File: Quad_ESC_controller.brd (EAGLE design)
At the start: 25.8 x 34.2 mm, 27 parts, among them IC1 OP-AMP, Y1 ECS-80-S-4X

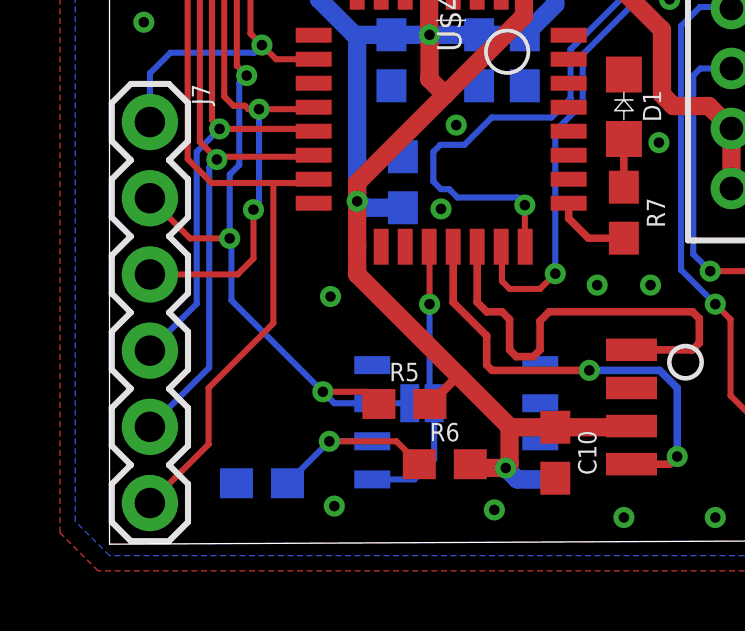
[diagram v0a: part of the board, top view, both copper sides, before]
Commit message: fixed stupid jumper under chip mistake
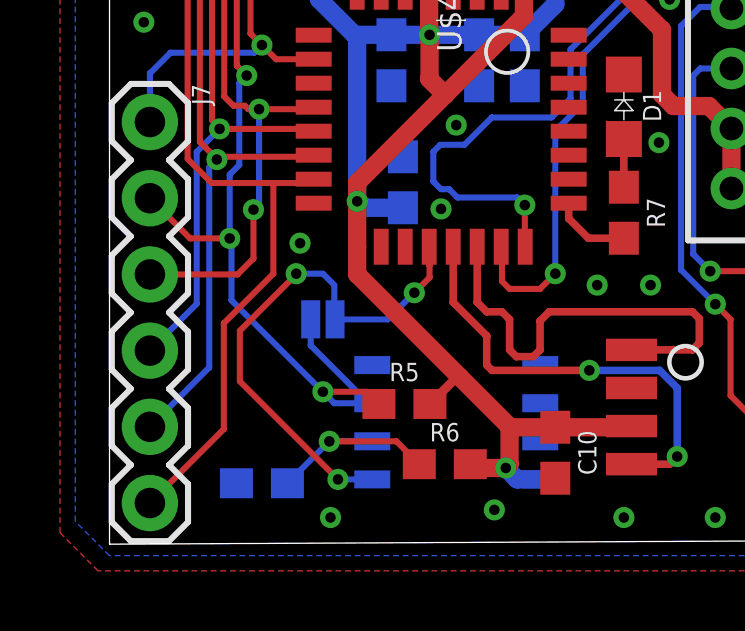
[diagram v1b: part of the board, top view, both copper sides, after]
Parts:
- moved JP1 4.33 mm to (7.11, 7.49)
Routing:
- net TLM: track 9.50 -> 17.5 mm, vias 1 -> 3
- net TLM_ESC: track 34.2 -> 36.7 mm
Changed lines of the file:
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@@
 <attribute name="VALUE" x="5.08" y="2.794" size="0.6096" layer="28" font="vector" ratio="20" rot="MR180" align="top-center"/>
 </element>
-<element name="JP1" library="SparkFun-Jumpers" library_urn="urn:adsk.eagle:library:528" package="SMT-JUMPER_2_NO_SILK" package3d_urn="urn:adsk.eagle:package:39279/1" value="JUMPER-SMT_2_NO_SILK" x="10.414" y="4.699" smashed="yes" rot="MR180">
-<attribute name="NAME" x="10.414" y="3.556" size="0.6096" layer="26" font="vector" ratio="20" rot="MR180" align="bottom-center"/>
+<element name="JP1" library="SparkFun-Jumpers" library_urn="urn:adsk.eagle:library:528" package="SMT-JUMPER_2_NO_SILK" package3d_urn="urn:adsk.eagle:package:39279/1" value="JUMPER-SMT_2_NO_SILK" x="7.112" y="7.493" smashed="yes" rot="MR180">
+<attribute name="NAME" x="7.112" y="6.35" size="0.6096" layer="26" font="vector" ratio="20" rot="MR180" align="bottom-center"/>
 </element>
 <element name="J7" library="SparkFun-Connectors" library_urn="urn:adsk.eagle:library:513" package="1X06" package3d_urn="urn:adsk.eagle:package:38009/1" value="" x="1.3462" y="14.0716" smashed="yes" rot="R270">
@@
 <via x="20.193" y="0.889" extent="1-16" drill="0.35"/>
 <via x="17.145" y="0.889" extent="1-16" drill="0.35"/>
-<via x="7.493" y="1.27" extent="1-16" drill="0.35"/>
+<via x="7.366" y="0.889" extent="1-16" drill="0.35"/>
 <via x="12.827" y="1.143" extent="1-16" drill="0.35"/>
 <contactref element="IC1" pad="4"/>
 <contactref element="R8" pad="1"/>
-<via x="7.366" y="8.255" extent="1-16" drill="0.35"/>
+<via x="6.35" y="10.033" extent="1-16" drill="0.35"/>
 </signal>
 <signal name="+3V3">
@@
 <contactref element="J7" pad="6"/>
 <wire x1="2.6042" y1="12.839" x2="3.4052" y2="12.038" width="0.2032" layer="1"/>
-<wire x1="1.3462" y1="1.3716" x2="3.302" y2="3.3274" width="0.2032" layer="1"/>
-<wire x1="3.302" y1="3.3274" x2="3.302" y2="5.207" width="0.2032" layer="1"/>
-<wire x1="5.461" y1="7.366" x2="5.461" y2="12.038" width="0.2032" layer="1"/>
-<wire x1="3.302" y1="5.207" x2="5.461" y2="7.366" width="0.2032" layer="1"/>
+<wire x1="1.3462" y1="1.3716" x2="3.81" y2="3.8354" width="0.2032" layer="1"/>
+<wire x1="3.81" y1="3.8354" x2="3.81" y2="7.366" width="0.2032" layer="1"/>
+<wire x1="5.461" y1="9.017" x2="5.461" y2="12.038" width="0.2032" layer="1"/>
+<wire x1="3.81" y1="7.366" x2="5.461" y2="9.017" width="0.2032" layer="1"/>
 </signal>
 <signal name="CAN_H">
@@
 <signal name="TLM">
 <contactref element="U$4" pad="PA10"/>
-<wire x1="10.655" y1="9.915" x2="10.668" y2="9.902" width="0.2032" layer="1"/>
-<wire x1="10.668" y1="9.902" x2="10.668" y2="8.001" width="0.2032" layer="1"/>
+<wire x1="10.655" y1="9.915" x2="10.655" y2="9.306" width="0.2032" layer="1"/>
+<wire x1="10.668" y1="9.293" x2="10.655" y2="9.306" width="0.2032" layer="1"/>
+<wire x1="10.668" y1="9.293" x2="10.668" y2="8.89" width="0.2032" layer="1"/>
+<wire x1="10.668" y1="8.89" x2="10.16" y2="8.382" width="0.2032" layer="1"/>
 <contactref element="IC1" pad="1"/>
 <contactref element="JP1" pad="2"/>
-<wire x1="8.757" y1="2.159" x2="10.16" y2="2.159" width="0.2032" layer="16"/>
-<via x="10.668" y="8.001" extent="1-16" drill="0.35"/>
-<wire x1="10.8204" y1="2.8194" x2="10.8204" y2="4.699" width="0.2032" layer="16"/>
-<wire x1="10.16" y1="2.159" x2="10.8204" y2="2.8194" width="0.2032" layer="16"/>
-<wire x1="10.8204" y1="4.699" x2="10.668" y2="4.8514" width="0.2032" layer="16"/>
-<wire x1="10.668" y1="4.8514" x2="10.668" y2="8.001" width="0.2032" layer="16"/>
+<via x="10.16" y="8.382" extent="1-16" drill="0.35"/>
+<wire x1="8.757" y1="2.159" x2="7.614" y2="2.159" width="0.2032" layer="16"/>
+<wire x1="7.614" y1="2.159" x2="4.3434" y2="5.4296" width="0.2032" layer="1"/>
+<wire x1="4.3434" y1="5.4296" x2="4.3434" y2="7.112" width="0.2032" layer="1"/>
+<wire x1="10.16" y1="8.382" x2="9.271" y2="7.493" width="0.2032" layer="16"/>
+<wire x1="9.271" y1="7.493" x2="7.5184" y2="7.493" width="0.2032" layer="16"/>
+<via x="7.614" y="2.159" extent="1-16" drill="0.35"/>
+<wire x1="7.5184" y1="7.493" x2="7.493" y2="7.5184" width="0.2032" layer="16"/>
+<wire x1="7.493" y1="7.5184" x2="7.493" y2="8.636" width="0.2032" layer="16"/>
+<wire x1="7.493" y1="8.636" x2="7.112" y2="9.017" width="0.2032" layer="16"/>
+<wire x1="7.112" y1="9.017" x2="6.223" y2="9.017" width="0.2032" layer="16"/>
+<via x="6.223" y="9.017" extent="1-16" drill="0.35"/>
+<wire x1="6.223" y1="8.9916" x2="6.223" y2="9.017" width="0.2032" layer="1"/>
+<wire x1="4.3434" y1="7.112" x2="6.223" y2="8.9916" width="0.2032" layer="1"/>
 </signal>
 <signal name="ADC">
@@
 <wire x1="7.112" y1="5.08" x2="8.5734" y2="5.08" width="0.2032" layer="1"/>
 <wire x1="8.5734" y1="5.08" x2="8.9798" y2="4.6736" width="0.2032" layer="1"/>
-<wire x1="10.0076" y1="4.699" x2="8.757" y2="4.699" width="0.2032" layer="16"/>
+<wire x1="6.7056" y1="7.493" x2="6.7056" y2="6.6234" width="0.2032" layer="16"/>
+<wire x1="8.63" y1="4.699" x2="6.7056" y2="6.6234" width="0.2032" layer="16"/>
+<wire x1="8.63" y1="4.699" x2="8.757" y2="4.699" width="0.2032" layer="16"/>
 <contactref element="J7" pad="2"/>
 <wire x1="4.2418" y1="27.4482" x2="4.2418" y2="15.9512" width="0.2032" layer="1"/>
